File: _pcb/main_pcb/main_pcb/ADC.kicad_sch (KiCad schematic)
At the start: 5 parts, among them U2 74HC4051

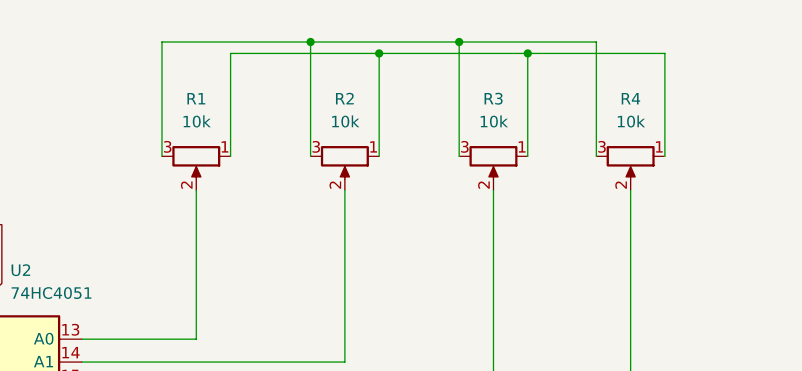
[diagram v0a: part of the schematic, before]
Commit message: for now the last commit for pcb as buying pcb is too expensive
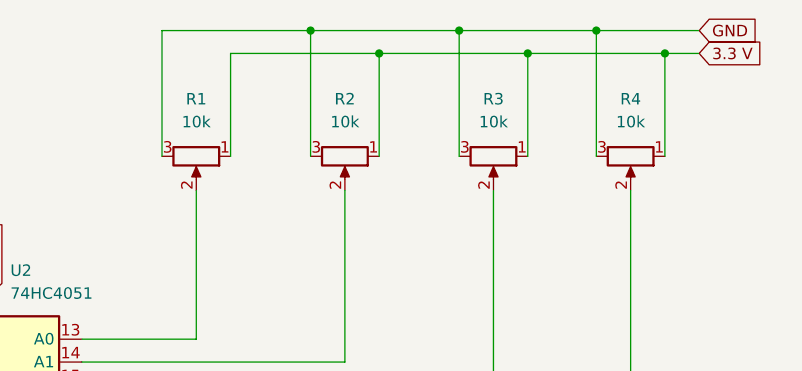
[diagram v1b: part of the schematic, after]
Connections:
- net GND: now also R1.3, R2.3, R3.3, R4.3
- net 3.3 V: now reaches R1.1, R2.1, R3.1, R4.1
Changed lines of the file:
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@@
 	)
 	(junction
-		(at 214.63 39.37)
+		(at 214.63 38.1)
+		(diameter 0)
+		(color 0 0 0 0)
+	)
+	(junction
+		(at 198.12 38.1)
 		(diameter 0)
 		(color 0 0 0 0)
@@
 	)
 	(junction
+		(at 229.87 38.1)
+		(diameter 0)
+		(color 0 0 0 0)
+	)
+	(junction
+		(at 237.49 40.64)
+		(diameter 0)
+		(color 0 0 0 0)
+	)
+	(junction
 		(at 162.56 95.25)
 		(diameter 0)
 		(color 0 0 0 0)
 	)
-	(junction
-		(at 198.12 39.37)
-		(diameter 0)
-		(color 0 0 0 0)
-	)
 	(wire
 		(pts
@@
 	(wire
 		(pts
+			(xy 237.49 40.64) (xy 241.3 40.64)
+		)
+		(stroke
+			(width 0)
+			(type default)
+		)
+	)
+	(wire
+		(pts
 			(xy 205.74 40.64) (xy 222.25 40.64)
 		)
@@
 	(wire
 		(pts
+			(xy 198.12 38.1) (xy 198.12 52.07)
+		)
+		(stroke
+			(width 0)
+			(type default)
+		)
+	)
+	(wire
+		(pts
 			(xy 172.72 80.01) (xy 233.68 80.01)
 		)
@@
 	(wire
 		(pts
-			(xy 214.63 39.37) (xy 229.87 39.37)
-		)
-		(stroke
-			(width 0)
-			(type default)
-		)
-	)
-	(wire
-		(pts
-			(xy 198.12 39.37) (xy 214.63 39.37)
+			(xy 214.63 38.1) (xy 229.87 38.1)
+		)
+		(stroke
+			(width 0)
+			(type default)
+		)
+	)
+	(wire
+		(pts
+			(xy 198.12 38.1) (xy 214.63 38.1)
 		)
 		(stroke
@@
 	(wire
 		(pts
-			(xy 198.12 39.37) (xy 198.12 52.07)
+			(xy 214.63 38.1) (xy 214.63 52.07)
 		)
 		(stroke
@@
 	(wire
 		(pts
-			(xy 214.63 39.37) (xy 214.63 52.07)
-		)
-		(stroke
-			(width 0)
-			(type default)
-		)
-	)
-	(wire
-		(pts
 			(xy 172.72 77.47) (xy 218.44 77.47)
 		)
@@
 	(wire
 		(pts
-			(xy 181.61 52.07) (xy 181.61 39.37)
+			(xy 181.61 52.07) (xy 181.61 38.1)
 		)
 		(stroke
@@
 	(wire
 		(pts
+			(xy 229.87 38.1) (xy 241.3 38.1)
+		)
+		(stroke
+			(width 0)
+			(type default)
+		)
+	)
+	(wire
+		(pts
 			(xy 218.44 77.47) (xy 218.44 55.88)
 		)
@@
 	(wire
 		(pts
-			(xy 181.61 39.37) (xy 198.12 39.37)
+			(xy 181.61 38.1) (xy 198.12 38.1)
 		)
 		(stroke
@@
 	(wire
 		(pts
-			(xy 229.87 39.37) (xy 229.87 52.07)
+			(xy 229.87 38.1) (xy 229.87 52.07)
 		)
 		(stroke
@@
 			(width 0)
 			(type default)
+		)
+	)
+	(global_label "3.3 V"
+		(shape input)
+		(at 241.3 40.64 0)
+		(fields_autoplaced yes)
+		(effects
+			(font
+				(size 1.27 1.27)
+			)
+			(justify left)
+		)
+		(property "Intersheetrefs" "${INTERSHEET_REFS}"
+			(at 249.3652 40.64 0)
+			(effects
+				(font
+					(size 1.27 1.27)
+				)
+				(justify left)
+				(hide yes)
+			)
 		)
 	)
@@
 				(hide yes)
 			)
+		)
+	)
+	(global_label "GND"
+		(shape input)
+		(at 241.3 38.1 0)
+		(fields_autoplaced yes)
+		(effects
+			(font
+				(size 1.27 1.27)
+			)
+			(justify left)
+		)
+		(property "Intersheetrefs" "${INTERSHEET_REFS}"
+			(at 248.1557 38.1 0)
+			(effects
+				(font
+					(size 1.27 1.27)
+				)
+				(justify left)
+				(hide yes)
+			)

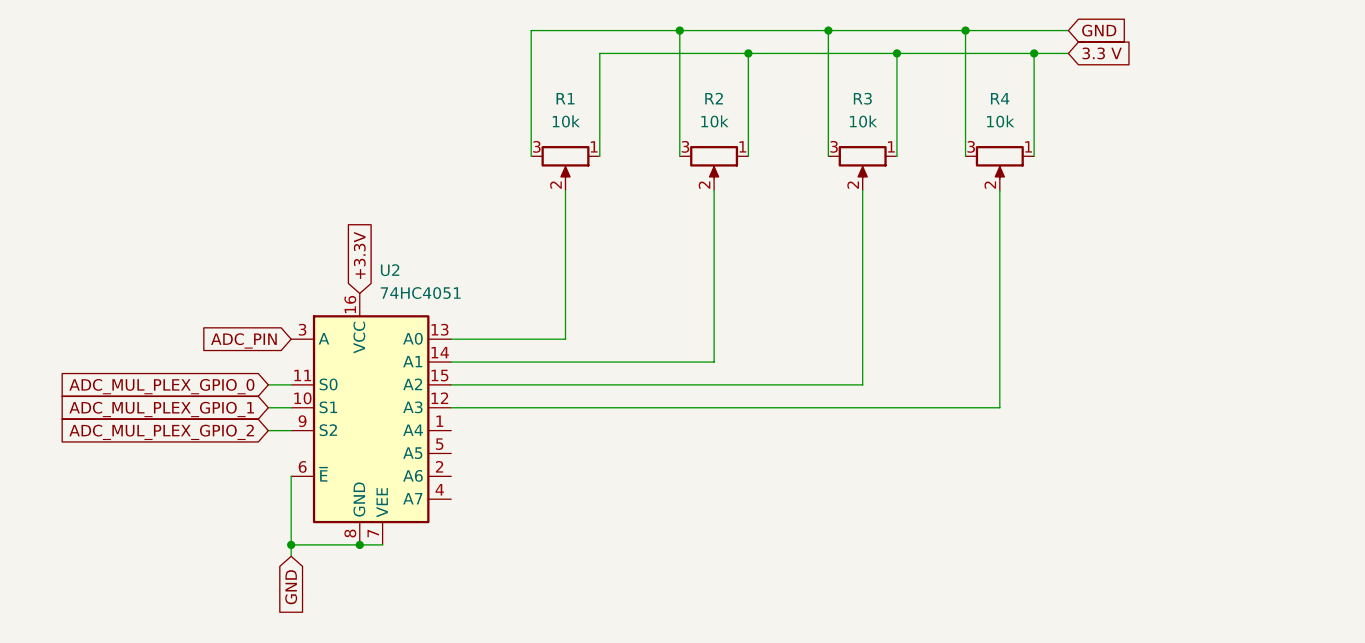
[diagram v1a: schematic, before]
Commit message: added leds to io expander
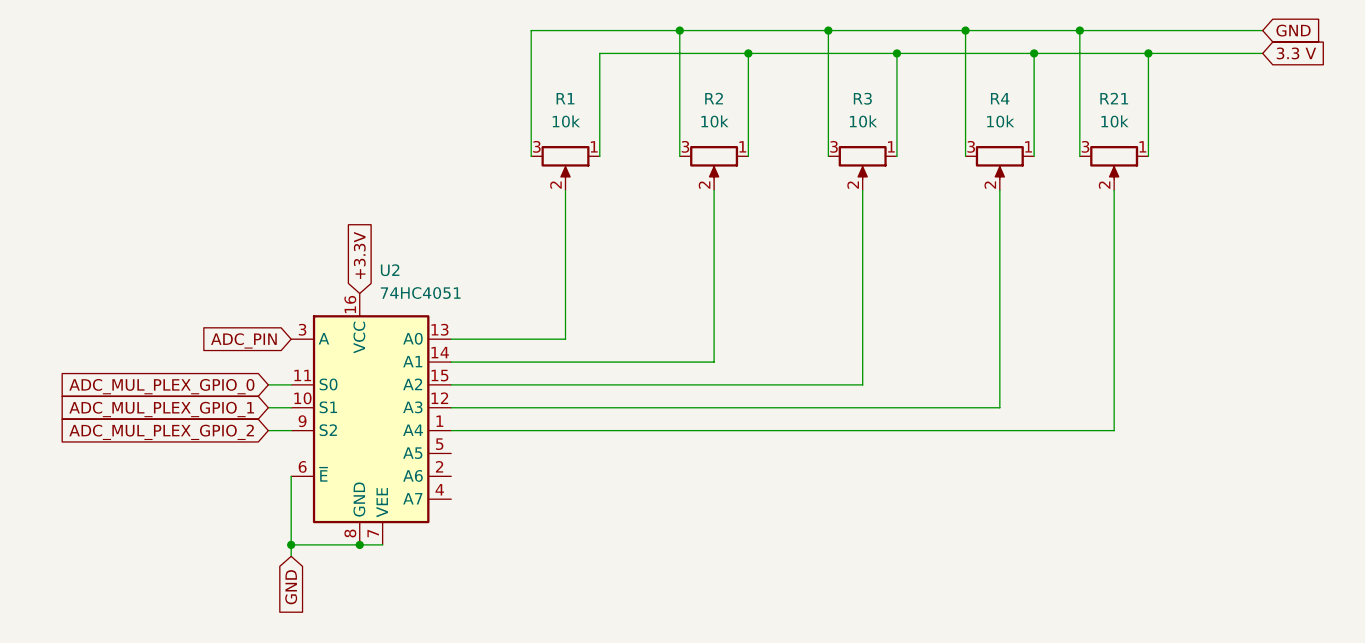
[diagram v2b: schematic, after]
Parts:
- added R21: 10k, Potentiometer:Linear_Potentiometer, symbol Device:R_Potentiometer
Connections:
- net 3.3 V: now also R21.1
- net GND: now also R21.3
- net at U2.1 (A4): now also R21.2
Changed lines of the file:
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@@
+	)
+	(junction
+		(at 250.19 40.64)
+		(diameter 0)
+		(color 0 0 0 0)
 	)
 	(junction
@@
 		(color 0 0 0 0)
 	)
+	(junction
+		(at 242.57 38.1)
+		(diameter 0)
+		(color 0 0 0 0)
+	)
 	(wire
 		(pts
@@
 	(wire
 		(pts
+			(xy 246.38 55.88) (xy 246.38 82.55)
+		)
+		(stroke
+			(width 0)
+			(type default)
+		)
+	)
+	(wire
+		(pts
 			(xy 152.4 82.55) (xy 154.94 82.55)
 		)
@@
 	(wire
 		(pts
-			(xy 237.49 40.64) (xy 241.3 40.64)
+			(xy 250.19 40.64) (xy 262.89 40.64)
+		)
+		(stroke
+			(width 0)
+			(type default)
+		)
+	)
+	(wire
+		(pts
+			(xy 237.49 40.64) (xy 250.19 40.64)
 		)
 		(stroke
@@
 	(wire
 		(pts
+			(xy 250.19 40.64) (xy 250.19 52.07)
+		)
+		(stroke
+			(width 0)
+			(type default)
+		)
+	)
+	(wire
+		(pts
+			(xy 246.38 82.55) (xy 172.72 82.55)
+		)
+		(stroke
+			(width 0)
+			(type default)
+		)
+	)
+	(wire
+		(pts
 			(xy 172.72 74.93) (xy 201.93 74.93)
 		)
@@
 	(wire
 		(pts
-			(xy 229.87 38.1) (xy 241.3 38.1)
+			(xy 229.87 38.1) (xy 242.57 38.1)
 		)
 		(stroke
@@
 	(wire
 		(pts
+			(xy 242.57 38.1) (xy 242.57 52.07)
+		)
+		(stroke
+			(width 0)
+			(type default)
+		)
+	)
+	(wire
+		(pts
 			(xy 185.42 72.39) (xy 172.72 72.39)
 		)
@@
 	(wire
 		(pts
+			(xy 242.57 38.1) (xy 262.89 38.1)
+		)
+		(stroke
+			(width 0)
+			(type default)
+		)
+	)
+	(wire
+		(pts
 			(xy 222.25 40.64) (xy 237.49 40.64)
 		)
@@
 	(global_label "3.3 V"
 		(shape input)
-		(at 241.3 40.64 0)
+		(at 262.89 40.64 0)
 		(fields_autoplaced yes)
 		(effects
@@
 		)
 		(property "Intersheetrefs" "${INTERSHEET_REFS}"
-			(at 249.3652 40.64 0)
+			(at 270.9552 40.64 0)
 			(effects
 				(font
@@
 	(global_label "GND"
 		(shape input)
-		(at 241.3 38.1 0)
+		(at 262.89 38.1 0)
 		(fields_autoplaced yes)
 		(effects
@@
 		)
 		(property "Intersheetrefs" "${INTERSHEET_REFS}"
-			(at 248.1557 38.1 0)
+			(at 269.7457 38.1 0)
 			(effects
 				(font
@@
 			)
 		)
+	)
+	(symbol
+		(lib_id "Device:R_Potentiometer")
+		(at 246.38 52.07 270)
+		(unit 1)
+		(exclude_from_sim no)
+		(in_bom yes)
+		(on_board yes)
+		(dnp no)
+		(fields_autoplaced yes)
+		(property "Reference" "R21"
+			(at 246.38 45.72 90)
+			(effects
+				(font
+					(size 1.27 1.27)
+				)
+			)
+		)
+		(property "Value" "10k"
+			(at 246.38 48.26 90)
+			(effects
+				(font
+					(size 1.27 1.27)
+				)
+			)
+		)
+		(property "Footprint" "Potentiometer:Linear_Potentiometer"
+			(at 246.38 52.07 0)
+			(effects
+				(font
+					(size 1.27 1.27)
+				)
+				(hide yes)
+			)
+		)
+		(property "Datasheet" "~"
+			(at 246.38 52.07 0)
+			(effects
+				(font
+					(size 1.27 1.27)
+				)
+				(hide yes)
+			)
+		)
+		(property "Description" "Potentiometer"
+			(at 246.38 52.07 0)
+			(effects
+				(font
+					(size 1.27 1.27)
+				)
+				(hide yes)
+			)
+		)
+		(pin "3"
+		)
+		(pin "1"
+		)
+		(pin "2"
+		)
+		(instances
+			(project "main_pcb"
+				(path "/b764235d-842d-41df-960a-a32e4258c2ec/f23f292d-bce7-4f3d-8f4f-e415aa1ad861"
+					(reference "R21")
+					(unit 1)
+				)
+			)
+		)

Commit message: changed ICs to THT
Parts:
- U2: footprint Package_DIP:SMDIP-16_W9.53mm -> Package_DIP:DIP-16_W7.62mm
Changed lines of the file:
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@@
 			)
 		)
-		(property "Footprint" "Package_DIP:SMDIP-16_W9.53mm"
+		(property "Footprint" "Package_DIP:DIP-16_W7.62mm"
 			(at 162.56 90.17 0)
 			(effects

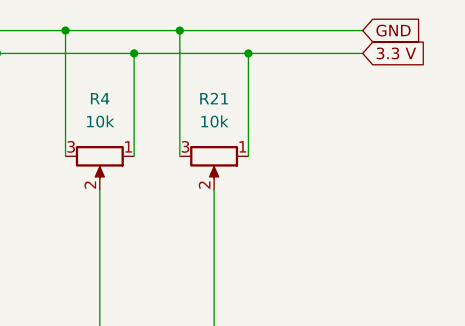
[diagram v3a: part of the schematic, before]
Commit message: changed 3.3 V and 0 V so that it is correct
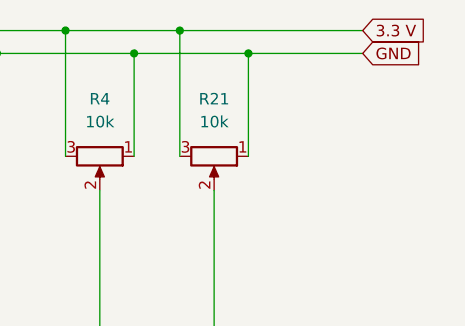
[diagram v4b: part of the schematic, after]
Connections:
- net 3.3 V: now also R1.3, R2.3, R21.3, R3.3, R4.3; no longer R1.1, R2.1, R21.1, R3.1, R4.1
- net GND: now also R1.1, R2.1, R21.1, R3.1, R4.1; no longer R1.3, R2.3, R21.3, R3.3, R4.3
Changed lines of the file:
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@@
 	(global_label "3.3 V"
 		(shape input)
-		(at 262.89 40.64 0)
+		(at 262.89 38.1 0)
 		(fields_autoplaced yes)
 		(effects
@@
 		)
 		(property "Intersheetrefs" "${INTERSHEET_REFS}"
-			(at 270.9552 40.64 0)
+			(at 270.9552 38.1 0)
 			(effects
 				(font
@@
 	(global_label "GND"
 		(shape input)
-		(at 262.89 38.1 0)
+		(at 262.89 40.64 0)
 		(fields_autoplaced yes)
 		(effects
@@
 		)
 		(property "Intersheetrefs" "${INTERSHEET_REFS}"
-			(at 269.7457 38.1 0)
+			(at 269.7457 40.64 0)
 			(effects
 				(font
